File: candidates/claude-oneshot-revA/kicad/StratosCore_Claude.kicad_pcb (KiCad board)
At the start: 4 copper layers, 60 x 84 mm, 277 parts, among them J1 USB4105-GF-A, J2 BM12B-GHS-TBT (expansion), J3 XF3M-4015-1B (TFT 40p FPC), J4 XF3M-0615-1B (CTP 6p FPC), J5 U.FL-R-SMT-1(60) GNSS, J6 U.FL-R-SMT-1(60) LoRa, J7 U.FL-R-SMT-1(60) ADS-B, J8 DM3AT-SF-PEJM5, Q1 Dual N-MOSFET TBD (O05), Q2 2N7002, SW1 SKSCLCE010 (BUTTON_1 / BOOT), SW2 SKSCLCE010 (BUTTON_2), U1 ESP32-S3-WROOM-1-N16R8, U10 TPS22918DBVR, U11 TPS22918DBVR, U12 TPS22918DBVR, U13 TCA9535PWR, U14 SN74AXC4T245PWR, U15 SN74LVC1G07DBVR, U16 TPS61169DCKR, U17 MAX-M10S-00B, U2 TPD4E05U06DQAR, U20 RP2040, U21 W25Q128JVSIQ, U23 TPD4E05U06DQAR, U24 TXU0202DCUR, U3 TPS259474LRPWR, U30 ICM-42688-P, U31 MMC5983MA, U32 BMP581, U33 SHT40-AD1B-R2, U4 TUSB320LAIRWBR, U40 SX1262IMLTRT, U41 PE4259, U5 S-8252 (product code TBD, O05), U50 BLB01, U52 BLB01, U54 ADL5513ACPZ-R7, U55 MCP6566T-E/OT, U6 BQ25887RGER, U7 TPS62130ARGTR, U8 TPS7A2030PDBVR, U9 TPS7A2018PDBVR, Y1 12MHz ABM8-272-T3, Y2 32 MHz (CL 10pF) MPN TBD

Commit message: docs: show one-shot candidate renders and schematic in README, fix 3D models
Root README gains a status table for the Claude one-shot candidate, 3D and
enclosure renders, PCB copper view, all 12 schematic sheets as images and
step-by-step instructions (folders) to open the KiCad project or the STEP
files. Candidate README gets the same gallery and KiCad instructions.

3D: envelope STEP models for parts whose footprint had no model in the
KiCad 10.0.6 install (MAX-M10S, ICM-42688-P, MMC5983MA, BMP581, TPD1E0B04,
TPS259474L RPW, TUSB320LAI, Coilcraft inductors, SHT40), so the board STEP
and the Alt+3 view are complete. Routing unchanged; DRC 1 reviewed error,
11 unconnected, parity 0.

Co-Authored-By: Claude Opus 5.5 <noreply@anthropic.com>
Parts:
- L2: footprint Inductor_SMD:L_Coilcraft_XxL4020 -> SC:L_Coilcraft_XxL4020
- L3: footprint Inductor_SMD:L_Coilcraft_LPS4018 -> SC:L_Coilcraft_LPS4018
- U33: footprint Sensor_Humidity:Sensirion_DFN-4_1.5x1.5mm_P0.8mm_SHT4x_NoCentralPad -> SC:Sensirion_DFN-4_1.5x1.5mm_P0.8mm_SHT4x_NoCentralPad
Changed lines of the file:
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@@
 		)
 		(embedded_fonts no)
+		(model "${KIPRJMOD}/libs/SC.3dshapes/MEMSIC_MMC5983MA_LGA-16_3x3mm_P0.5mm_CORRECTED.step"
+			(offset
+				(xyz 0 0 0)
+			)
+			(scale
+				(xyz 1 1 1)
+			)
+			(rotate
+				(xyz 0 0 0)
+			)
+		)
 	)
 	(footprint "Package_TO_SOT_SMD:SOT-23"
@@
 		)
 		(embedded_fonts no)
+		(model "${KIPRJMOD}/libs/SC.3dshapes/Bosch_BMP581_LGA-10_2x2mm_CORRECTED.step"
+			(offset
+				(xyz 0 0 0)
+			)
+			(scale
+				(xyz 1 1 1)
+			)
+			(rotate
+				(xyz 0 0 0)
+			)
+		)
 	)
 	(footprint "SC:Hirose_U.FL-R-SMT-1_60_Vertical"
@@
 		)
 		(embedded_fonts no)
-		(model "${KICAD10_3DMODEL_DIR}/Package_DFN_QFN.3dshapes/QFN-16-1EP_3x3mm_P0.5mm_EP1.75x1.75mm.step"
+		(model "${KICAD10_3DMODEL_DIR}/Package_DFN_QFN.3dshapes/UQFN-16-1EP_3x3mm_P0.5mm_EP1.75x1.75mm.step"
 			(offset
 				(xyz 0 0 0)
@@
 		)
 		(embedded_fonts no)
-		(model "${KICAD10_3DMODEL_DIR}/Package_DFN_QFN.3dshapes/Texas_X2QFN-12_1.6x1.6mm_P0.4mm.step"
+		(model "${KIPRJMOD}/libs/SC.3dshapes/TI_RWB0012B_X2QFN-12_1.6x1.6mm_TUSB320LAI.step"
 			(offset
 				(xyz 0 0 0)
@@
 		)
 		(embedded_fonts no)
+		(model "${KIPRJMOD}/libs/SC.3dshapes/TI_TPD1E0B04DPYR_X1SON-2_DPY0002A.step"
+			(offset
+				(xyz 0 0 0)
+			)
+			(scale
+				(xyz 1 1 1)
+			)
+			(rotate
+				(xyz 0 0 0)
+			)
+		)
 	)
 	(footprint "Inductor_SMD:L_0402_1005Metric"
@@
 		)
 		(embedded_fonts no)
+		(model "${KIPRJMOD}/libs/SC.3dshapes/TI_TPD1E0B04DPYR_X1SON-2_DPY0002A.step"
+			(offset
+				(xyz 0 0 0)
+			)
+			(scale
+				(xyz 1 1 1)
+			)
+			(rotate
+				(xyz 0 0 0)
+			)
+		)
 	)
 	(footprint "Resistor_SMD:R_0402_1005Metric"
@@
 		)
 		(embedded_fonts no)
-		(model "${KICAD10_3DMODEL_DIR}/Package_DFN_QFN.3dshapes/Texas_RPU0010A_VQFN-HR-10_2x2mm_P0.5mm.step"
+		(model "${KIPRJMOD}/libs/SC.3dshapes/TI_RPW0010A_VQFN-HR-10_2x2mm_P0.45mm.step"
 			(offset
 				(xyz 0 0 0)
@@
 		(embedded_fonts no)
 	)
-	(footprint "Sensor_Humidity:Sensirion_DFN-4_1.5x1.5mm_P0.8mm_SHT4x_NoCentralPad"
+	(footprint "SC:Sensirion_DFN-4_1.5x1.5mm_P0.8mm_SHT4x_NoCentralPad"
 		(layer "F.Cu")
 		(at 44 1.9)
@@
 		)
 		(embedded_fonts no)
-		(model "${KICAD10_3DMODEL_DIR}/Sensor_Humidity.3dshapes/Sensirion_DFN-4_1.5x1.5mm_P0.8mm_SHT4x_NoCentralPad.step"
+		(model "${KIPRJMOD}/libs/SC.3dshapes/Sensirion_DFN-4_1.5x1.5mm_P0.8mm_SHT4x_NoCentralPad_SC.step"
 			(offset
 				(xyz 0 0 0)
@@
 		)
 	)
-	(footprint "Inductor_SMD:L_Coilcraft_LPS4018"
+	(footprint "SC:L_Coilcraft_LPS4018"
 		(layer "F.Cu")
 		(at 41.8 55.2)
@@
 		)
 		(embedded_fonts no)
-		(model "${KICAD10_3DMODEL_DIR}/Inductor_SMD.3dshapes/L_Coilcraft_LPS4018.step"
+		(model "${KIPRJMOD}/libs/SC.3dshapes/L_Coilcraft_LPS4018_SC.step"
 			(offset
 				(xyz 0 0 0)
@@
 		)
 		(embedded_fonts no)
+		(model "${KIPRJMOD}/libs/SC.3dshapes/u-blox_MAX-M10S-00B_LCC-18_10.1x9.7mm.step"
+			(offset
+				(xyz 0 0 0)
+			)
+			(scale
+				(xyz 1 1 1)
+			)
+			(rotate
+				(xyz 0 0 0)
+			)
+		)
 	)
 	(footprint "SC:Omron_XF3M-4015-1B_1x40-1MP_P0.5mm_Horizontal"
@@
 		(embedded_fonts no)
 	)
-	(footprint "Inductor_SMD:L_Coilcraft_XxL4020"
+	(footprint "SC:L_Coilcraft_XxL4020"
 		(layer "F.Cu")
 		(at 26.8 51.8)
@@
 		)
 		(embedded_fonts no)
-		(model "${KICAD10_3DMODEL_DIR}/Inductor_SMD.3dshapes/L_Coilcraft_XxL4020.step"
+		(model "${KIPRJMOD}/libs/SC.3dshapes/L_Coilcraft_XxL4020_SC.step"
 			(offset
 				(xyz 0 0 0)
@@
 		)
 		(embedded_fonts no)
+		(model "${KIPRJMOD}/libs/SC.3dshapes/TDK_ICM-42688-P_LGA-14_3x2.5mm_P0.5mm.step"
+			(offset
+				(xyz 0 0 0)
+			)
+			(scale
+				(xyz 1 1 1)
+			)
+			(rotate
+				(xyz 0 0 0)
+			)
+		)
 	)
 	(footprint "Fuse:Fuse_1206_3216Metric"
@@
 	)
 	(zone
-		(net "GND")
+		(net "3V3_MAIN")
 		(layer "In2.Cu")
 		(hatch edge 0.5)
-		(connect_pads yes
+		(priority 1)
+		(connect_pads
 			(clearance 0.2)
 		)
@@
 		(polygon
 			(pts
-				(xy 0.3 0.3) (xy 59.7 0.3) (xy 59.7 83.7) (xy 0.3 83.7)
+				(xy 19 27) (xy 59.7 27) (xy 59.7 78) (xy 44 78) (xy 44 64) (xy 19 64)
 			)
 		)
 	)
 	(zone
-		(net "3V3_MAIN")
+		(net "GND")
 		(layer "In2.Cu")
 		(hatch edge 0.5)
-		(priority 1)
-		(connect_pads
+		(connect_pads yes
 			(clearance 0.2)
 		)
@@
 		(polygon
 			(pts
-				(xy 19 27) (xy 59.7 27) (xy 59.7 78) (xy 44 78) (xy 44 64) (xy 19 64)
+				(xy 0.3 0.3) (xy 59.7 0.3) (xy 59.7 83.7) (xy 0.3 83.7)
 			)
 		)

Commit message: candidates: evidence-backed refinement of the Claude one-shot KiCad candidate
Reviewed on origin/main e1f75a3 with KiCad 10.0.6; changes stay inside
candidates/claude-oneshot-revA/ and close no project gate.

- TXU0202 U24: exact TI DCU0008A land (SCES942A pp.32-34) replaces the
  generic KiCad DCU footprint; schematic/symbol footprint fields updated.
- TPS259474L U3 RPW: copper verified against the TI 4225183/A vectors;
  paste now follows the TI stencil example, fab body 2.0 mm.
- ICM-42688-P pin 9 tied to GND (TDK DS-000347 v1.9 Table 10).
- U1/J5 body-courtyard overlap fixed, duplicate vias removed, BMP581
  under-body SCL route removed, SHT40 SDA and 3V3 fragments connected,
  three GND islands stitched, C57 connected, silkscreen refined.
- Removed the unreviewed mask-bridge suppression on U30/U32; findings
  are now visible pending assembler review.
- Before/after ERC, DRC+parity, unconnected and net/pad reconciliation
  reports plus docs/REFINEMENT_2026_09_23.md. Remaining: floating GND at
  U2/U3/U24, SX1262 RF blocker, O05 and the other open gates.

Co-Authored-By: Claude Opus 5.5 <noreply@anthropic.com>
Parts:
- U24: footprint Package_SO:VSSOP-8_2.3x2mm_P0.5mm -> SC:TI_DCU0008A_VSSOP-8_2.3x2mm_P0.5mm_TXU0202
- moved C57 3.97 mm to (16.8, 43.1), turned to 90 degrees
- moved J5 0.40 mm to (29.4, 2.90)
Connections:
- U30 pad 9: unconnected-(U30-INT2/FSYNC-Pad9) -> GND
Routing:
- net I2C_SDA: track 187.0 -> 194.1 mm, vias 10 -> 11
- net I2C_SCL: track 209.6 -> 202.9 mm, vias 12 -> 11
- net 3V3_MAIN: track 491.2 -> 492.6 mm
- net GND: track 654.2 -> 655.6 mm, vias 282 -> 285
- net LED_A: track 38.5 -> 38.4 mm, vias 5 -> 4

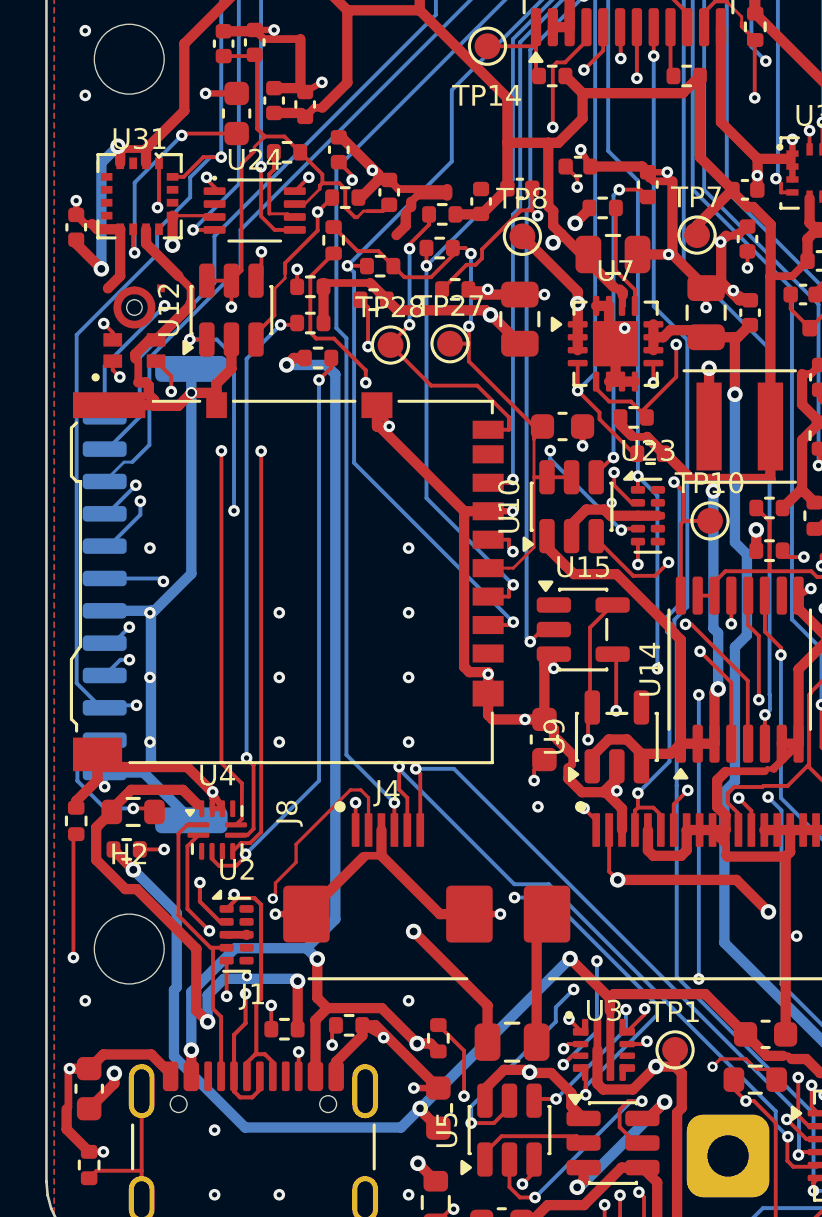
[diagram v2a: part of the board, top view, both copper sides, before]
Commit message: candidates: close floating grounds, swap TPS62130A to RGT0016C, add review notes
Integrates the parallel review work on the Claude one-shot candidate
(candidates/ only; no baseline, locked decision or gate changed):

- GND of U2 (USB ESD), U3 pad 8 (eFuse) and U24 pad 2 connected by local
  re-layout; U7 exposed pad now has 4 vias; GND is one copper group.
- U7 swapped to the TI RGT0016C land (SLVSAG7F p.41) and schematic field
  updated; J1 +0.3 mm move tried and reverted (collides in USB corner).
- Review notes: ESP32/USB-C/buttons audit (all 41 module pads verified),
  TPS62130A footprint, SX1262 E449 native values (topology redraw needed),
  GPIO A5-A8 options (owner decision), assembler mask rules and a dated
  cost snapshot (BRL 200 target infeasible on current parts).
- Final checks: unconnected 2 (SX1262 RF blocker only), parity 0,
  970 pins / 0 mismatches; remaining DRC errors are the U30/U32 mask
  bridges pending the assembler decision.

Co-Authored-By: Claude Opus 5.5 <noreply@anthropic.com>
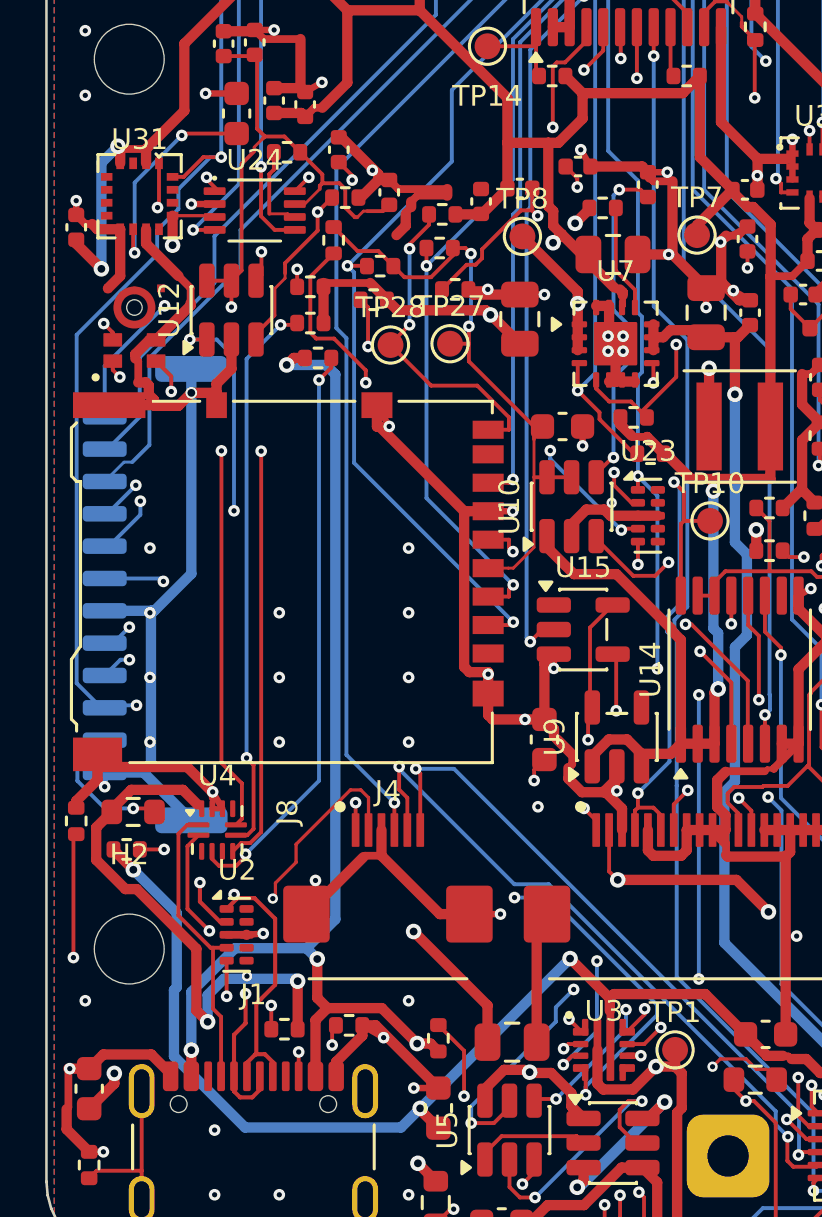
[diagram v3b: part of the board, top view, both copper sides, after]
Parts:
- U7: footprint SC:TI_RGT0016A_VQFN-16_3x3mm_EP1.75x1.75_TPS62130A -> SC:TI_RGT0016C_VQFN-16_3x3mm_EP1.68x1.68_TPS62130A
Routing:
- net GND: track 655.6 -> 657.0 mm, vias 285 -> 291
- net BUCK_SW: track 13.6 -> 14.5 mm
- net SD_CT: track 12.7 -> 13.4 mm
